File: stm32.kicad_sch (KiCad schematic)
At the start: 58 parts, among them J1 USB_B_Mini, J4 Conn_ST_STDC14, J5 Conn_02x05_Counter_Clockwise, J7 TC2030 - TAG Connect, SW1 SW_Push, SW2 SW_Push, U3 STM32F427V_G-I_Tx, X1 8MHz 20pF

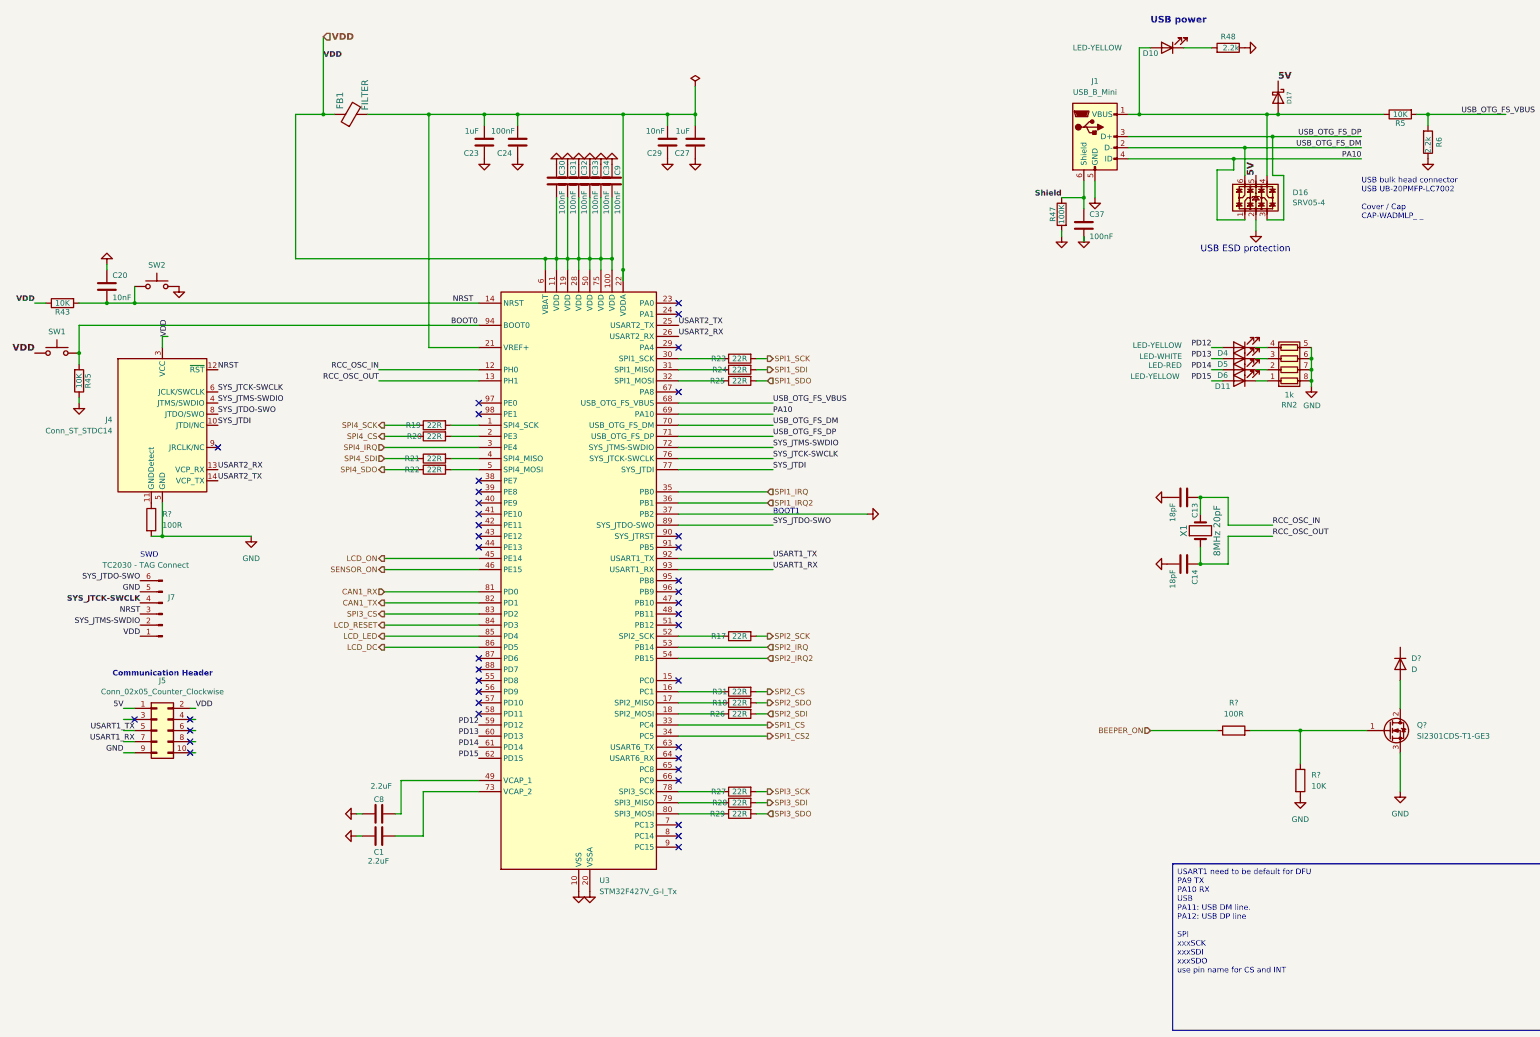
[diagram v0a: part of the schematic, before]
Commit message: change power add buzzer
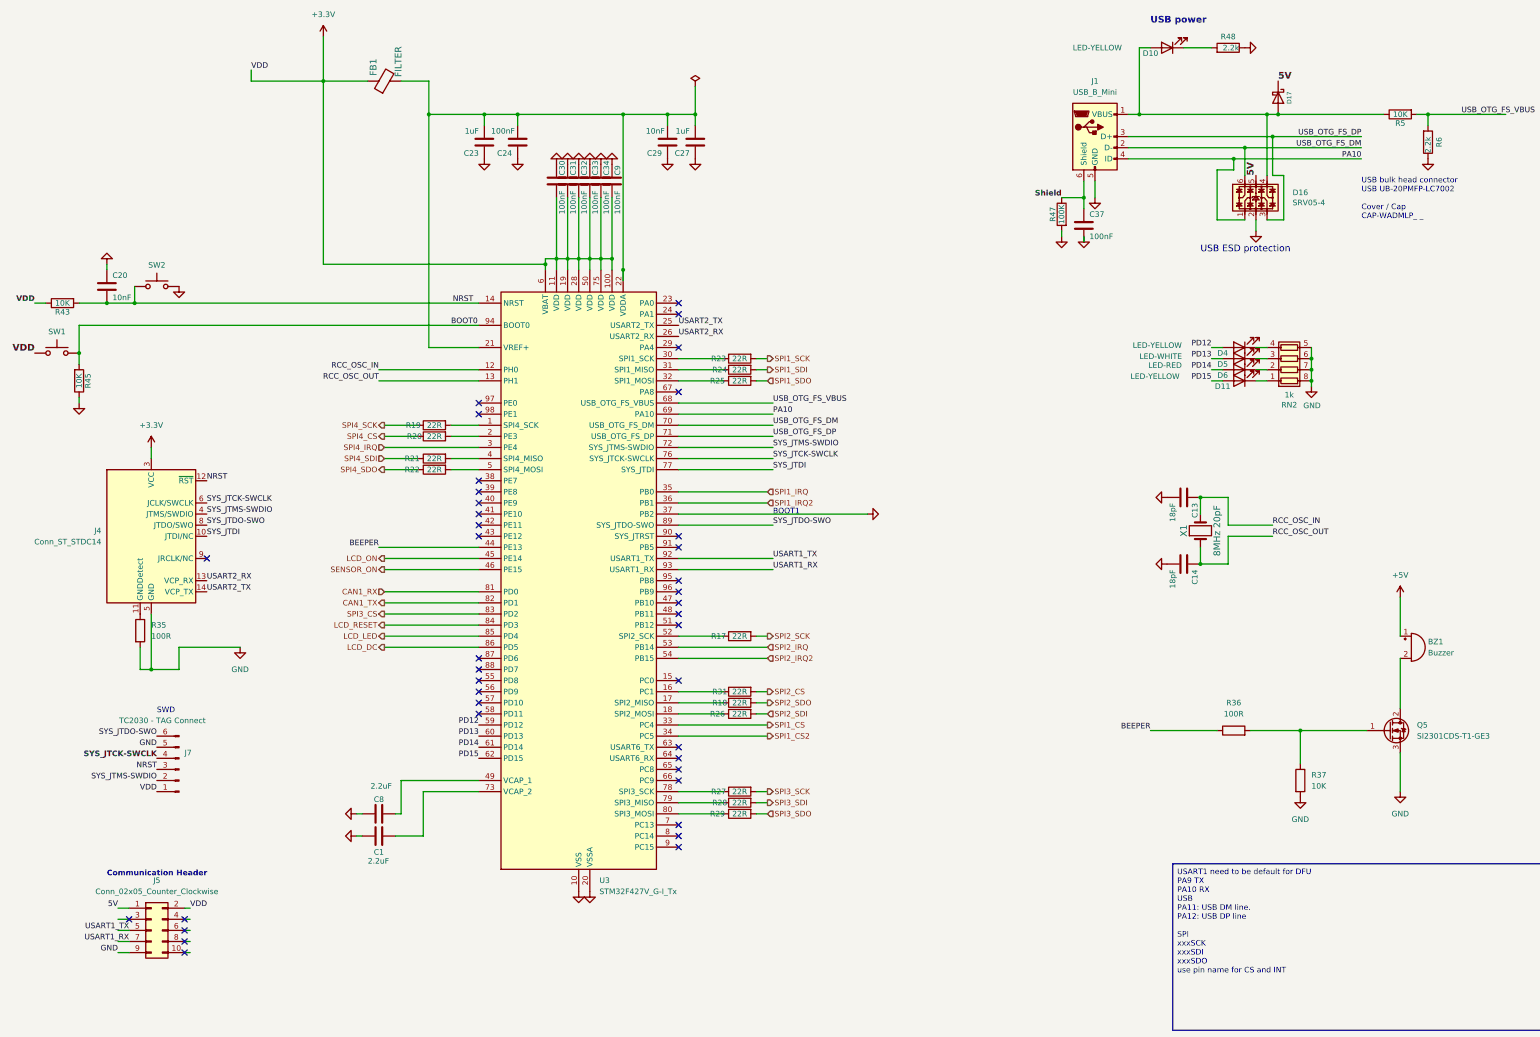
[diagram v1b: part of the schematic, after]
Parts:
- removed D?: D, Diode_SMD:D_SOD-123F, symbol Device:D
- added BZ1: Buzzer, dnt:Buzzer_9x9.5RM5.0, symbol Device:Buzzer
- gave numbers to parts that had none: 4
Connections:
- net BEEPER_ON is gone; now on net BEEPER: R36.1
- net at Q5.2 (D): now also BZ1.2 (-)
- net BEEPER: now reaches U3.44 (PE13)
- net VDD renamed +3.3V
- new net +5V: BZ1.1 (+)
- no-connect marks 40 -> 39
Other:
- moved on the sheet: FB1, J4, J5, J7, R35

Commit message: remove hellen
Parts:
- removed J5: Conn_02x05_Counter_Clockwise, Connector_PinHeader_2.54mm:PinHeader_2x05_P2.54mm_Vertical_SMD, symbol Connector_Generic:Conn_02x05_Odd_Even
- removed R36: 100R, symbol Device:R
- removed R37: 10K, symbol Device:R
- added R32: 100R, Resistor_SMD:R_0603_1608Metric, symbol Device:R
- added R33: 10K, Resistor_SMD:R_0603_1608Metric, symbol Device:R
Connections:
- net +3.3V: no longer J7.1 (Pin_1), R43.1, SW1.1
- net BEEPER: now also R32.2
- net GND: now also R33.1
- net at Q5.1 (G): now also R32.1, R33.2
- net PB10: now reaches U3.47 (PB10)
- net PB11: now reaches U3.48 (PB11)
- net PB12: now reaches U3.51 (PB12)
- net PB8: now reaches U3.95 (PB8)
- net PB9: now reaches U3.96 (PB9)
- new net VDD: J7.1 (Pin_1), R43.1, SW1.1
- no-connect marks 39 -> 28

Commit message: pre quilter
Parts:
- added J5: Conn_02x20_Odd_Even, Connector_PinSocket_2.54mm:PinSocket_2x20_P2.54mm_Vertical, symbol Connector_Generic:Conn_02x20_Odd_Even
- added R36: 10K, Resistor_SMD:R_0603_1608Metric, symbol Device:R
- J1: footprint hellen-one-common:USB-MINI-B-VERTICAL -> dnt:USB-MINI-B-VERTICAL; symbol hellen-one-common:USB_B_Mini -> Connector:USB_B_Mini
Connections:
- net 5V is gone; now on net +5V: D16.5, D17.1 (K)
- net VDD is gone; now on net +3.3V: J7.1 (Pin_1), R43.1, SW1.1
- net +3.3V: now also J5.8 (Pin_8)
- net GND: now also J5.4 (Pin_4), R36.1; no longer U3.37 (PB2)
- net PB10: now also J5.3 (Pin_3)
- net PB11: now also J5.5 (Pin_5)
- net PB12: now also J5.7 (Pin_7)
- net PB8: now also J5.10 (Pin_10)
- net PB9: now also J5.1 (Pin_1)
- net SYS_JTCK-SWCLK: now also J5.6 (Pin_6)
- net SYS_JTMS-SWDIO: now also J5.2 (Pin_2)
- net USART1_RX: now also J5.12 (Pin_12)
- net USART1_TX: now also J5.14 (Pin_14)
- net PC0: now reaches U3.15 (PC0)
- net PC0: now also J5.9 (Pin_9)
- net PA0: now reaches U3.23 (PA0)
- net PA0: now also J5.28 (Pin_28)
- net PA1: now reaches U3.24 (PA1)
- net PA1: now also J5.26 (Pin_26)
- net PA4: now reaches U3.29 (PA4)
- net PA4: now also J5.24 (Pin_24)
- net PE7: now reaches U3.38 (PE7)
- net PE7: now also J5.34 (Pin_34)
- net PE8: now reaches U3.39 (PE8)
- net PE8: now also J5.36 (Pin_36)
- net PE9: now reaches U3.40 (PE9)
- net PE9: now also J5.38 (Pin_38)
- net PE10: now reaches U3.41 (PE10)
- net PE10: now also J5.40 (Pin_40)
- net PE11: now reaches U3.42 (PE11)
- net PE11: now also J5.39 (Pin_39)
- net PE12: now reaches U3.43 (PE12)
- net PE12: now also J5.37 (Pin_37)
- net PD8: now reaches U3.55 (PD8)
- net PD8: now also J5.31 (Pin_31)
- net PD9: now reaches U3.56 (PD9)
- net PD9: now also J5.29 (Pin_29)
- net PD10: now reaches U3.57 (PD10)
- net PD10: now also J5.27 (Pin_27)
- net PD11: now reaches U3.58 (PD11)
- net PD11: now also J5.25 (Pin_25)
- net PC6: now reaches U3.63 (PC6)
- net PC6: now also J5.11 (Pin_11)
- net PC7: now reaches U3.64 (PC7)
- net PC7: now also J5.13 (Pin_13)
- net PC8: now reaches U3.65 (PC8)
- net PC8: now also J5.15 (Pin_15)
- net PC9: now reaches U3.66 (PC9)
- net PC9: now also J5.17 (Pin_17)
- net PA8: now reaches U3.67 (PA8)
- net PA8: now also J5.22 (Pin_22)
- net PC13: now reaches U3.7 (PC13)
- net PC13: now also J5.19 (Pin_19)
- net PC14: now reaches U3.8 (PC14)
- net PC14: now also J5.21 (Pin_21)
- net PD6: now reaches U3.87 (PD6)
- net PD6: now also J5.35 (Pin_35)
- net PD7: now reaches U3.88 (PD7)
- net PD7: now also J5.33 (Pin_33)
- net PC15: now reaches U3.9 (PC15)
- net PC15: now also J5.23 (Pin_23)
- net PB4: now reaches U3.90 (PB4)
- net PB4: now also J5.16 (Pin_16)
- net PB5: now reaches U3.91 (PB5)
- net PB5: now also J5.18 (Pin_18)
- net PE0: now reaches U3.97 (PE0)
- net PE0: now also J5.30 (Pin_30)
- net PE1: now reaches U3.98 (PE1)
- net PE1: now also J5.32 (Pin_32)
- new net BOOT1: J5.20 (Pin_20), R36.2, U3.37 (PB2)
- no-connect marks 28 -> 1
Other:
- note removed: "BOOT1"
- note removed: "Communication Header"
- note removed: "USB ESD protection"
- note removed: "USB bulk head connector USB UB-20PMFP-LC7002 Cover / Cap CAP-WADMLP_ _"
- moved on the sheet: J4, J7, R35
